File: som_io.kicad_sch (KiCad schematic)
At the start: 1 part, among them J1 Hermaphroditic_Molex_203456-0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

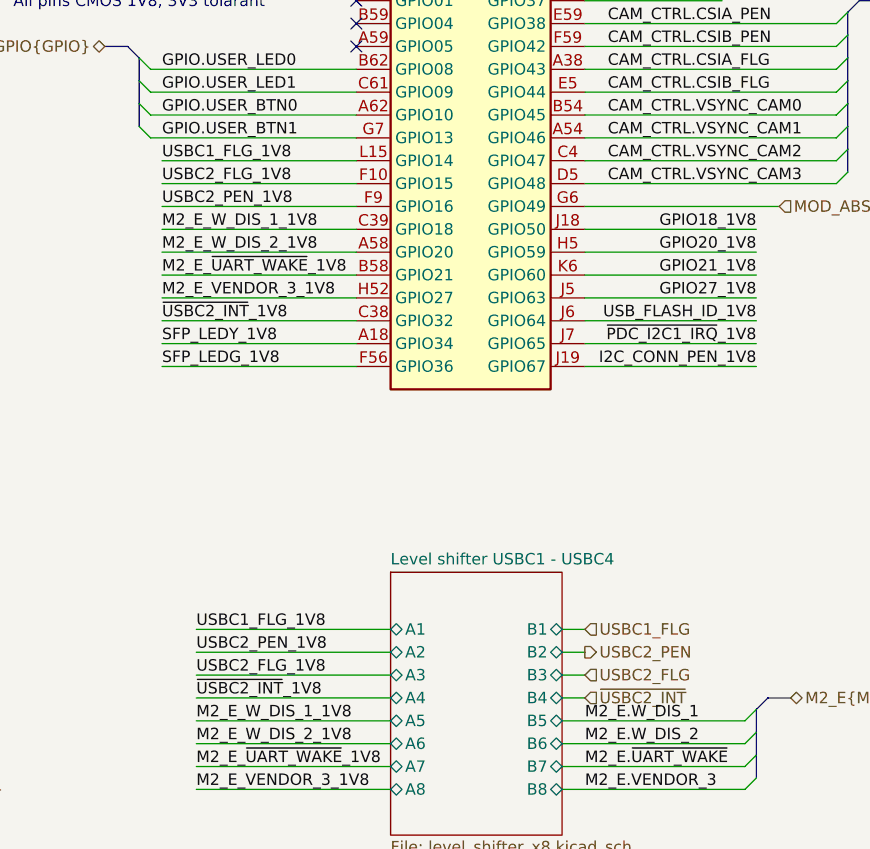
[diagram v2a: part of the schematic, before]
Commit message: [#85326] Fix USB-C 2 ID and enable handling
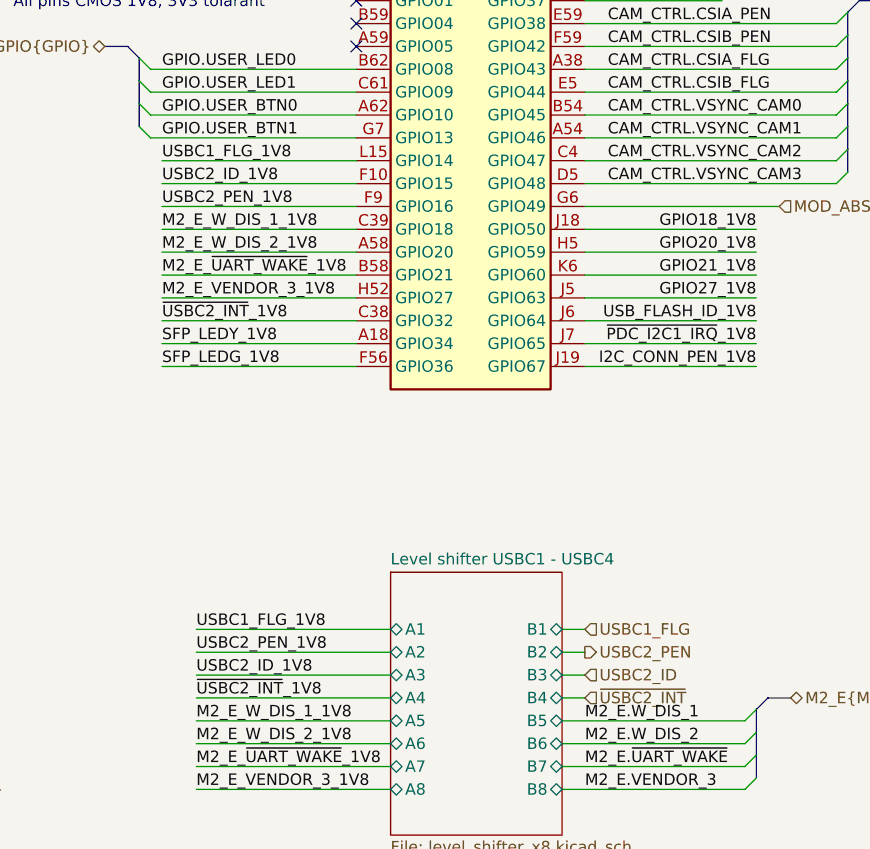
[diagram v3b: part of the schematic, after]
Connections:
- net USBC2_FLG_1V8 renamed USBC2_ID_1V8
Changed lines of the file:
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@@
 		)
 	)
-	(label "USBC2_FLG_1V8"
+	(label "USBC2_ID_1V8"
 		(at 193.04 55.88 0)
 		(effects
@@
 		)
 	)
-	(label "USBC2_FLG_1V8"
+	(label "USBC2_ID_1V8"
 		(at 196.85 110.49 0)
 		(effects
@@
 		)
 	)
+	(hierarchical_label "USBC2_ID"
+		(shape input)
+		(at 240.03 110.49 0)
+		(effects
+			(font
+				(size 1.27 1.27)
+			)
+			(justify left)
+		)
+	)
 	(hierarchical_label "UART2{UART}"
 		(shape bidirectional)
@@
 		(effects
 			(font
-				(size 1.27 1.27)
-			)
-			(justify left)
-		)
-	)
-	(hierarchical_label "USBC2_FLG"
-		(shape input)
-		(at 240.03 110.49 0)
-		(effects
-			(font

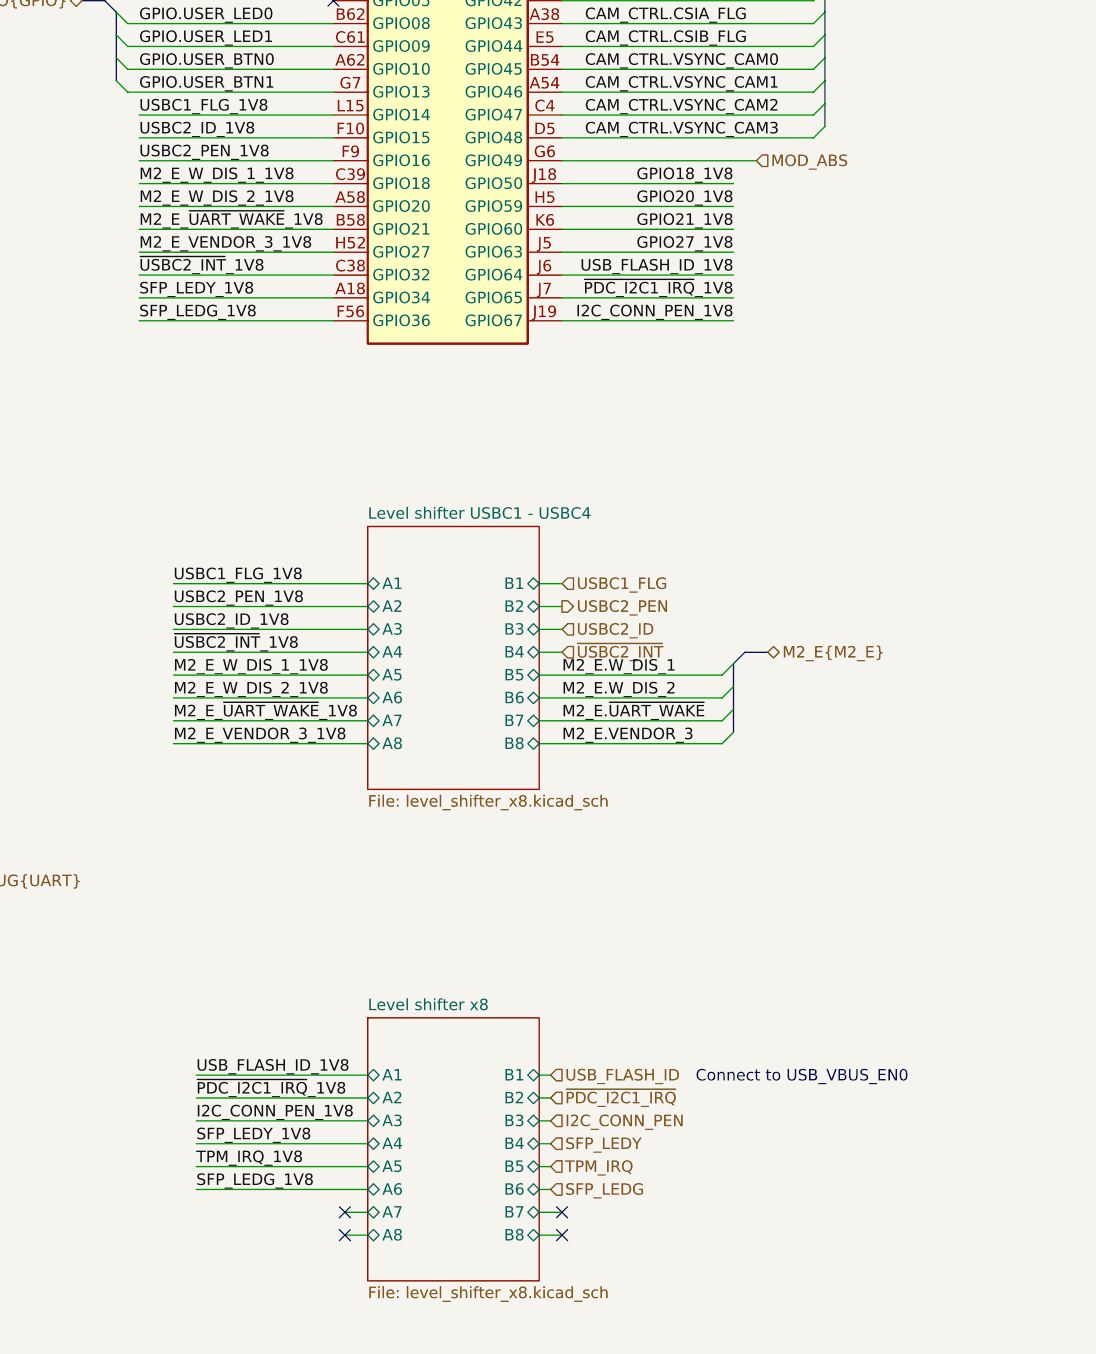
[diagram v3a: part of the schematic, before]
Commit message: [#85326] Improved USB-C 2 control signal connections
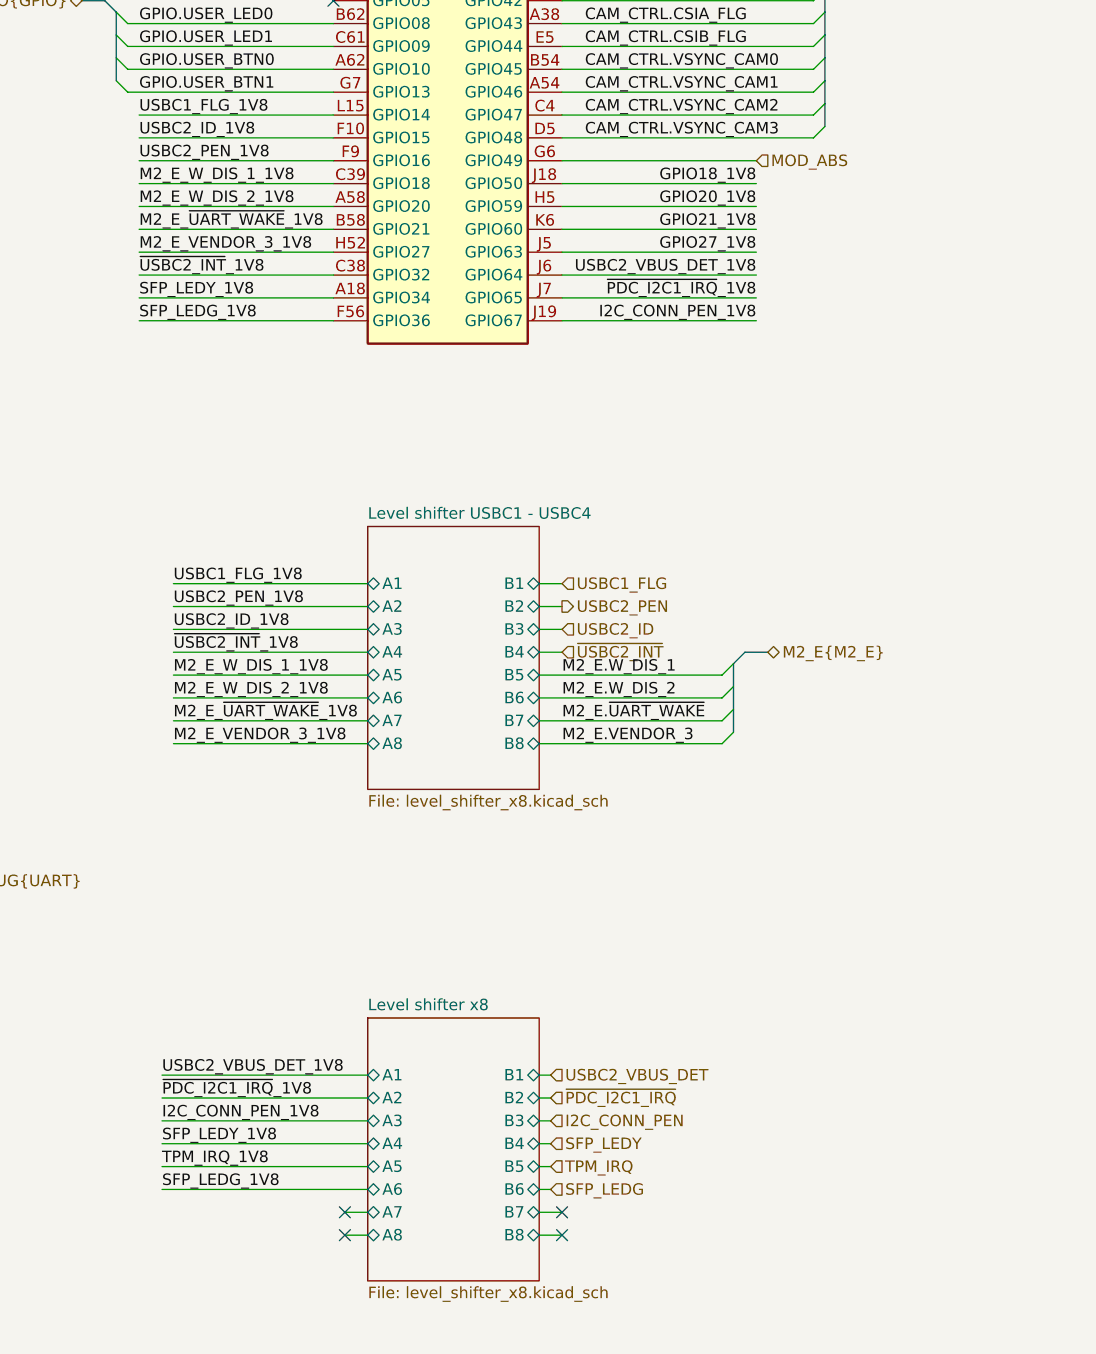
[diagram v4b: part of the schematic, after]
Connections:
- net USB_FLASH_ID_1V8 renamed USBC2_VBUS_DET_1V8
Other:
- note removed: "Connect to USB_VBUS_EN0"
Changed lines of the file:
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@@
 		)
 	)
-	(text "Connect to USB_VBUS_EN0"
-		(exclude_from_sim no)
-		(at 266.7 160.274 0)
-		(effects
-			(font
-				(size 1.27 1.27)
-			)
-		)
-	)
 	(text "All UART are \nCMOS - 1.8V"
 		(exclude_from_sim no)
@@
 	(wire
 		(pts
-			(xy 199.39 170.18) (xy 218.44 170.18)
+			(xy 195.58 170.18) (xy 218.44 170.18)
 		)
 		(stroke
@@
 	(wire
 		(pts
-			(xy 240.03 76.2) (xy 259.08 76.2)
+			(xy 240.03 76.2) (xy 261.62 76.2)
 		)
 		(stroke
@@
 	(wire
 		(pts
-			(xy 199.39 172.72) (xy 218.44 172.72)
+			(xy 195.58 172.72) (xy 218.44 172.72)
 		)
 		(stroke
@@
 	(wire
 		(pts
-			(xy 240.03 68.58) (xy 259.08 68.58)
+			(xy 240.03 68.58) (xy 261.62 68.58)
 		)
 		(stroke
@@
 	(wire
 		(pts
-			(xy 240.03 60.96) (xy 259.08 60.96)
+			(xy 240.03 60.96) (xy 261.62 60.96)
 		)
 		(stroke
@@
 	(wire
 		(pts
-			(xy 199.39 162.56) (xy 218.44 162.56)
+			(xy 195.58 162.56) (xy 218.44 162.56)
 		)
 		(stroke
@@
 	(wire
 		(pts
-			(xy 240.03 63.5) (xy 259.08 63.5)
+			(xy 240.03 63.5) (xy 261.62 63.5)
 		)
 		(stroke
@@
 	(wire
 		(pts
-			(xy 199.39 167.64) (xy 218.44 167.64)
+			(xy 195.58 167.64) (xy 218.44 167.64)
 		)
 		(stroke
@@
 	(wire
 		(pts
-			(xy 199.39 160.02) (xy 218.44 160.02)
+			(xy 195.58 160.02) (xy 218.44 160.02)
 		)
 		(stroke
@@
 	(wire
 		(pts
-			(xy 240.03 71.12) (xy 259.08 71.12)
+			(xy 240.03 71.12) (xy 261.62 71.12)
 		)
 		(stroke
@@
 	(wire
 		(pts
-			(xy 240.03 73.66) (xy 259.08 73.66)
+			(xy 240.03 73.66) (xy 261.62 73.66)
 		)
 		(stroke
@@
 	(wire
 		(pts
-			(xy 199.39 165.1) (xy 218.44 165.1)
+			(xy 195.58 165.1) (xy 218.44 165.1)
 		)
 		(stroke
@@
 	(wire
 		(pts
-			(xy 240.03 66.04) (xy 259.08 66.04)
+			(xy 240.03 66.04) (xy 261.62 66.04)
 		)
 		(stroke
@@
 	)
 	(label "GPIO27_1V8"
-		(at 259.08 68.58 180)
+		(at 261.62 68.58 180)
 		(effects
 			(font
@@
 		)
 	)
-	(label "USB_FLASH_ID_1V8"
-		(at 199.39 160.02 0)
+	(label "USBC2_VBUS_DET_1V8"
+		(at 195.58 160.02 0)
 		(effects
 			(font
@@
 	)
 	(label "GPIO18_1V8"
-		(at 259.08 60.96 180)
+		(at 261.62 60.96 180)
 		(effects
 			(font
@@
 	)
 	(label "SFP_LEDY_1V8"
-		(at 199.39 167.64 0)
+		(at 195.58 167.64 0)
 		(effects
 			(font
@@
 	)
 	(label "GPIO21_1V8"
-		(at 259.08 66.04 180)
+		(at 261.62 66.04 180)
 		(effects
 			(font
@@
 	)
 	(label "TPM_IRQ_1V8"
-		(at 199.39 170.18 0)
+		(at 195.58 170.18 0)
 		(effects
 			(font
@@
 	)
 	(label "I2C_CONN_PEN_1V8"
-		(at 259.08 76.2 180)
+		(at 261.62 76.2 180)
 		(effects
 			(font
@@
 	)
 	(label "~{PDC_I2C1_IRQ}_1V8"
-		(at 259.08 73.66 180)
+		(at 261.62 73.66 180)
 		(effects
 			(font
@@
 	)
 	(label "I2C_CONN_PEN_1V8"
-		(at 199.39 165.1 0)
+		(at 195.58 165.1 0)
 		(effects
 			(font
@@
 	)
 	(label "GPIO20_1V8"
-		(at 259.08 63.5 180)
+		(at 261.62 63.5 180)
 		(effects
 			(font
@@
 		)
 	)
-	(label "USB_FLASH_ID_1V8"
-		(at 259.08 71.12 180)
+	(label "USBC2_VBUS_DET_1V8"
+		(at 261.62 71.12 180)
 		(effects
 			(font
@@
 	)
 	(label "~{PDC_I2C1_IRQ}_1V8"
-		(at 199.39 162.56 0)
+		(at 195.58 162.56 0)
 		(effects
 			(font
@@
 	)
 	(label "SFP_LEDG_1V8"
-		(at 199.39 172.72 0)
+		(at 195.58 172.72 0)
 		(effects
 			(font
@@
 		)
 	)
-	(hierarchical_label "USB_FLASH_ID"
+	(hierarchical_label "USBC2_VBUS_DET"
 		(shape input)
 		(at 238.76 160.02 0)

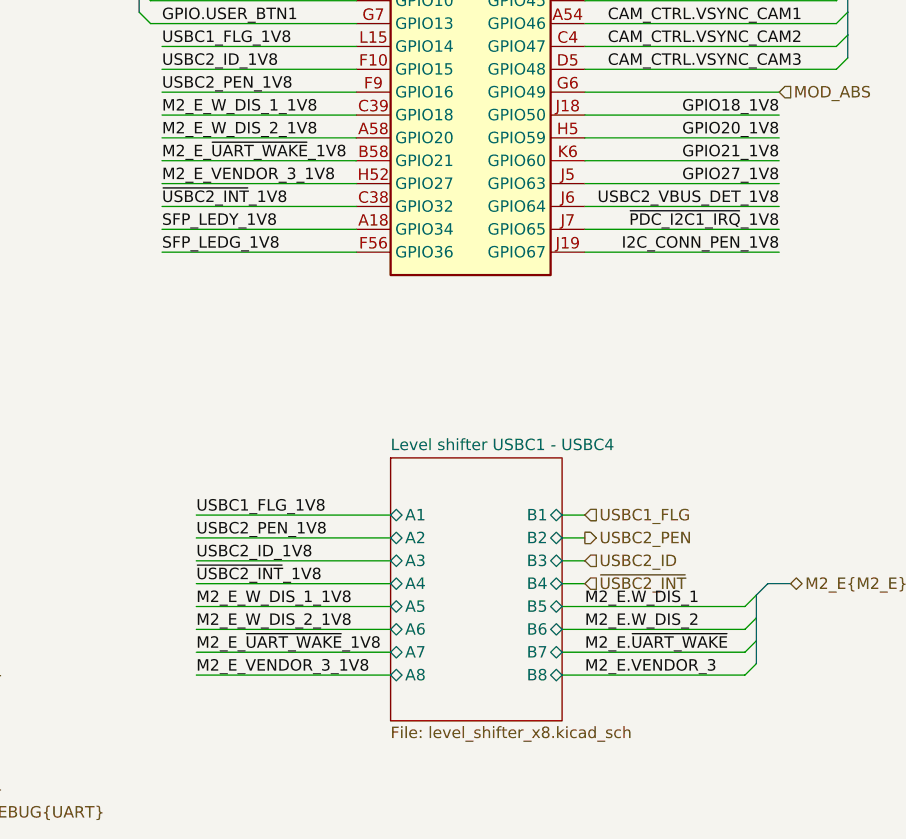
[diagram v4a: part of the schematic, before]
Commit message: [#85326] M.2 Key E fixes
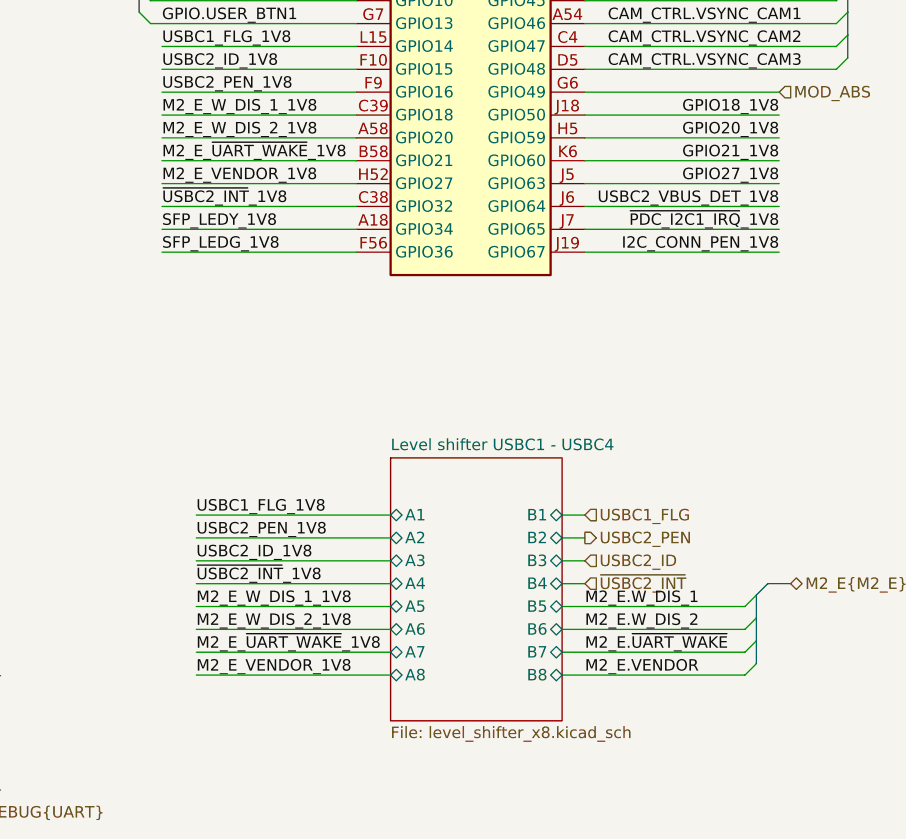
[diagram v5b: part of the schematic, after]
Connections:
- net M2_E_VENDOR_3_1V8 renamed M2_E_VENDOR_1V8
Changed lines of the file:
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@@
 	)
 	(bus_alias "M2_E"
-		(members "W_DIS_1" "W_DIS_2" "~{UART_WAKE}" "VENDOR_3")
+		(members "W_DIS_1" "W_DIS_2" "~{UART_WAKE}" "VENDOR")
 	)
 	(text "NOTE:\nDo not use as GPIO:\nGPIO42\nGPIO38\nGPIO37\nGPIO17"
@@
 		)
 	)
-	(label "M2_E.VENDOR_3"
+	(label "M2_E.VENDOR"
 		(at 240.03 123.19 0)
 		(effects
@@
 		)
 	)
-	(label "M2_E_VENDOR_3_1V8"
+	(label "M2_E_VENDOR_1V8"
 		(at 193.04 68.58 0)
 		(effects
@@
 		)
 	)
-	(label "M2_E_VENDOR_3_1V8"
+	(label "M2_E_VENDOR_1V8"
 		(at 196.85 123.19 0)
 		(effects
